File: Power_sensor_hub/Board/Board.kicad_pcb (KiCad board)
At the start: 2 copper layers, 101 x 84 mm, 92 parts, among them J1 ICSP, J2 USB_B_Micro, U1 ATmega32U4-A, U2 HC-SR04, U3 to-5V, U4 to-6V, U6 to-3V3, Y1 16MHz

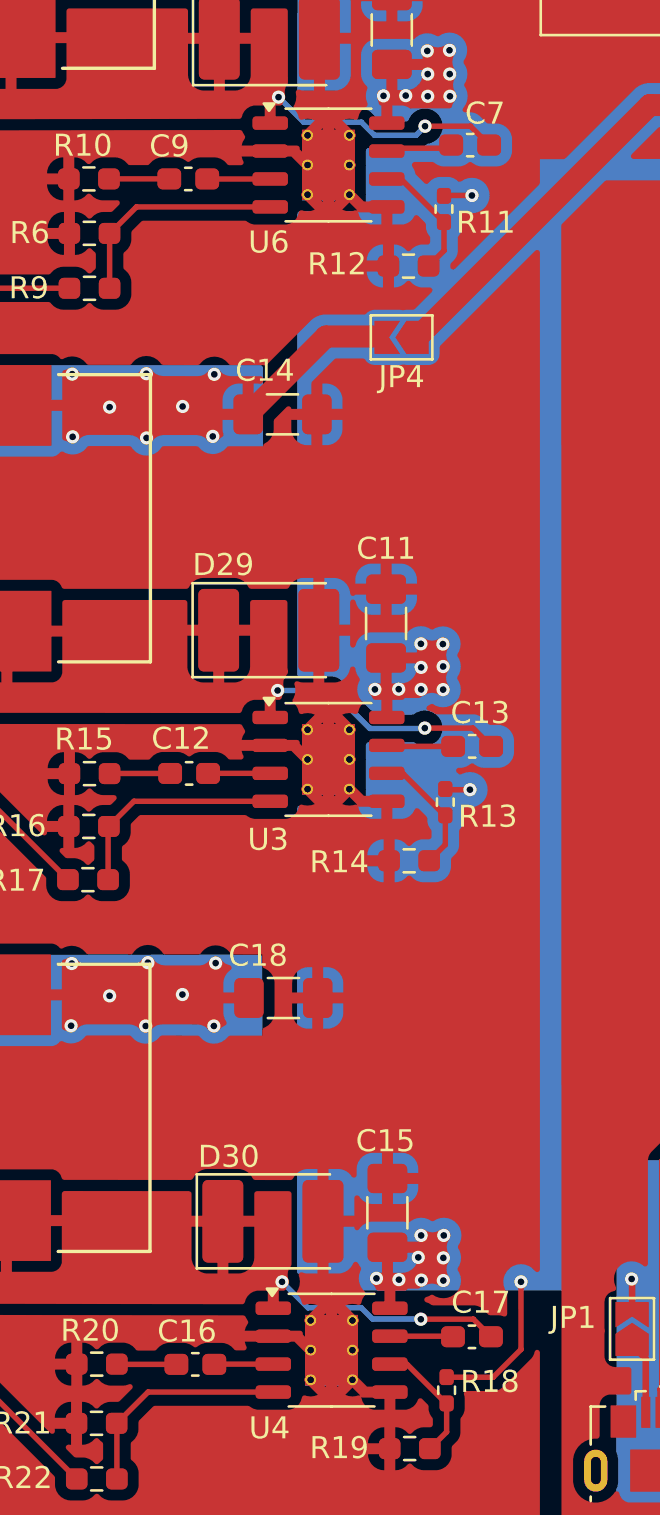
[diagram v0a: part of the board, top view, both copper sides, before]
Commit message: created skeleton/starter code
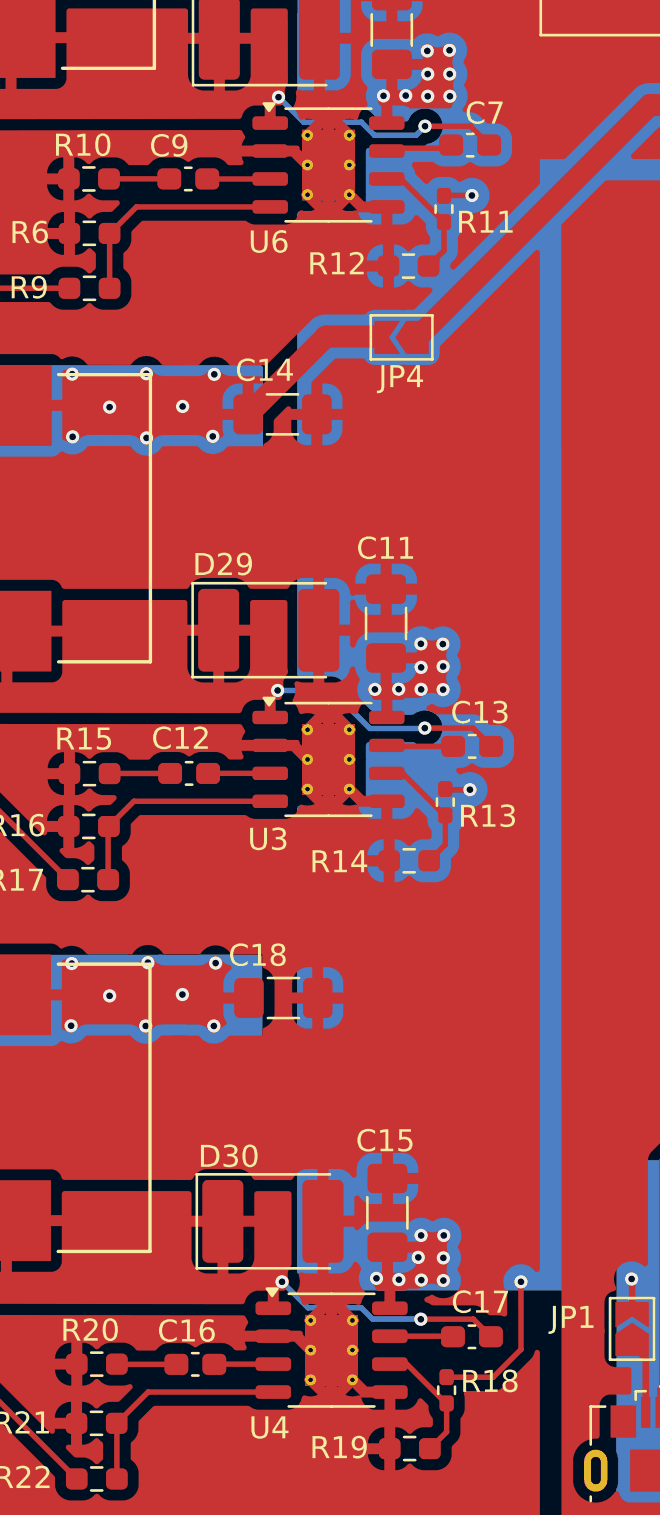
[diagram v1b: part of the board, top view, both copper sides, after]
